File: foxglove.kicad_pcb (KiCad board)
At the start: 4 copper layers, 70.7 x 53.3 mm, 167 parts, among them IC1 LFE5U-12F-6BG256C, J1 NEIGHBOR1, J2 NEIGHBOR2, J3 Conn_02x05_Odd_Even, J4 Conn_02x10_Odd_Even, J5 Conn_01x02_Female, J6 Conn_02x03_Odd_Even, J7 BONUS_ROW, U1 LM393, U10 SHIFTER, U11 74HC4051, U12 SHIFTER, U13 74HC4051, U14 SHIFTER, U15 74HC4051, U16 SHIFTER, U17 74HC4051, U18 SHIFTER, U19 74HC4051, U2 ADP225, U20 SHIFTER, U21 74HC4051, U22 SHIFTER, U23 74HC4051, U24 SHIFTER, U25 74LVC1G53, U26 PCA6408A, U3 AP2127, U4 74LVC1G3157, U5 AP2127, U6 AP2127, U7 DAC084S085, U8 AT25xxx, U9 74HC4051

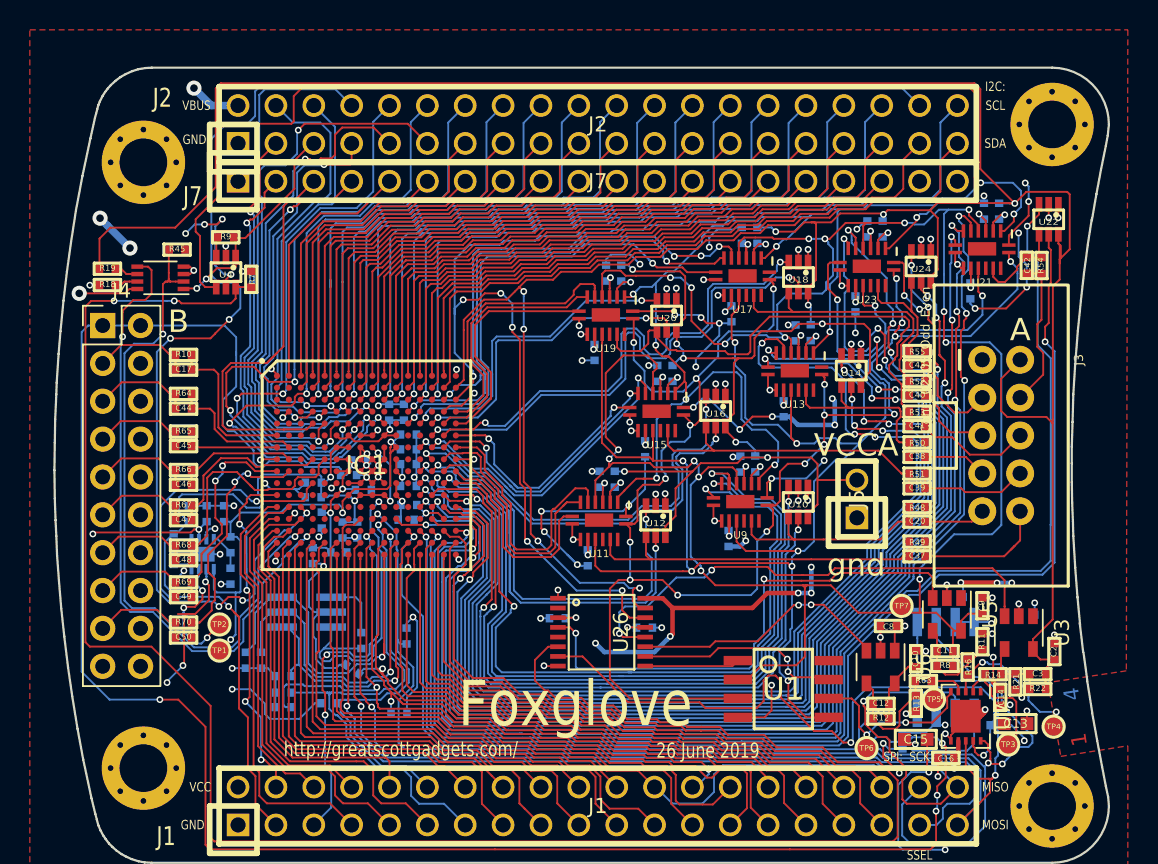
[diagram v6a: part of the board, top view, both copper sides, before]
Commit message: Matched path length of bank B differential pairs
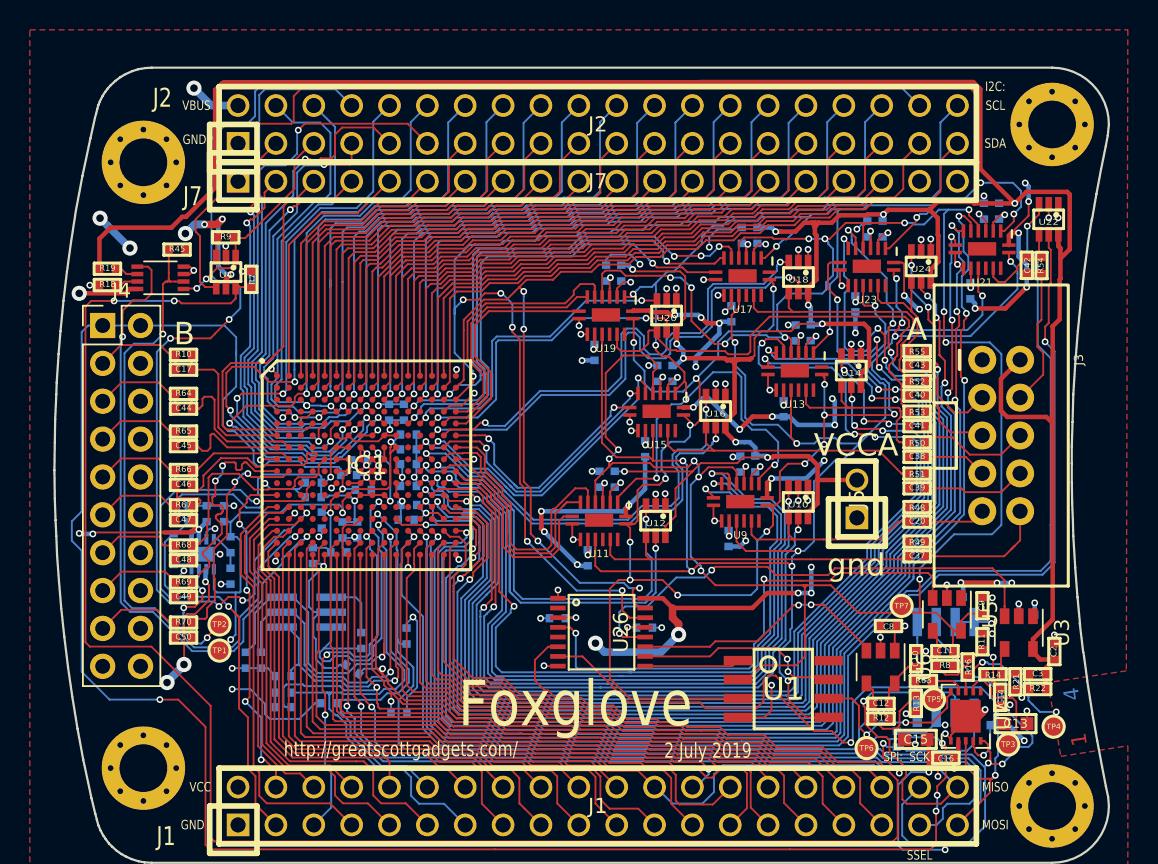
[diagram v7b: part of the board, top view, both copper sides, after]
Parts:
- moved R59 0.40 mm to (166.1, 113.6)
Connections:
- net /Sheet5D737161/target renamed /B1T_P
- net /sheet5D96E709/target renamed /B1T_N
- net /sheet5D9A1BD9/target renamed /B2T_P
- net /sheet5D9A1BDA/target renamed /B2T_N
- net /sheet5D9D50B4/target renamed /B3T_P
- net /sheet5D9D50B5/target renamed /B3T_N
- net /sheet5D9D50B6/target renamed /B4T_P
- net /sheet5D9D50B7/target renamed /B4T_N
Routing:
- net /VCCA: track 227.0 -> 263.0 mm
- net +5V: track 150.6 -> 160.2 mm, vias 52 -> 53
- net /B3_P: track 11.8 -> 15.9 mm
- net /B4_P: track 14.1 -> 16.2 mm
- net /B2_P: track 6.75 -> 8.20 mm
- net /B1_N: track 9.23 -> 10.7 mm
- net /J2.06: track 26.8 -> 26.9 mm, vias 2 -> 3
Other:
- board text added: "2 July 2019"
- board text removed: "26 June 2019"

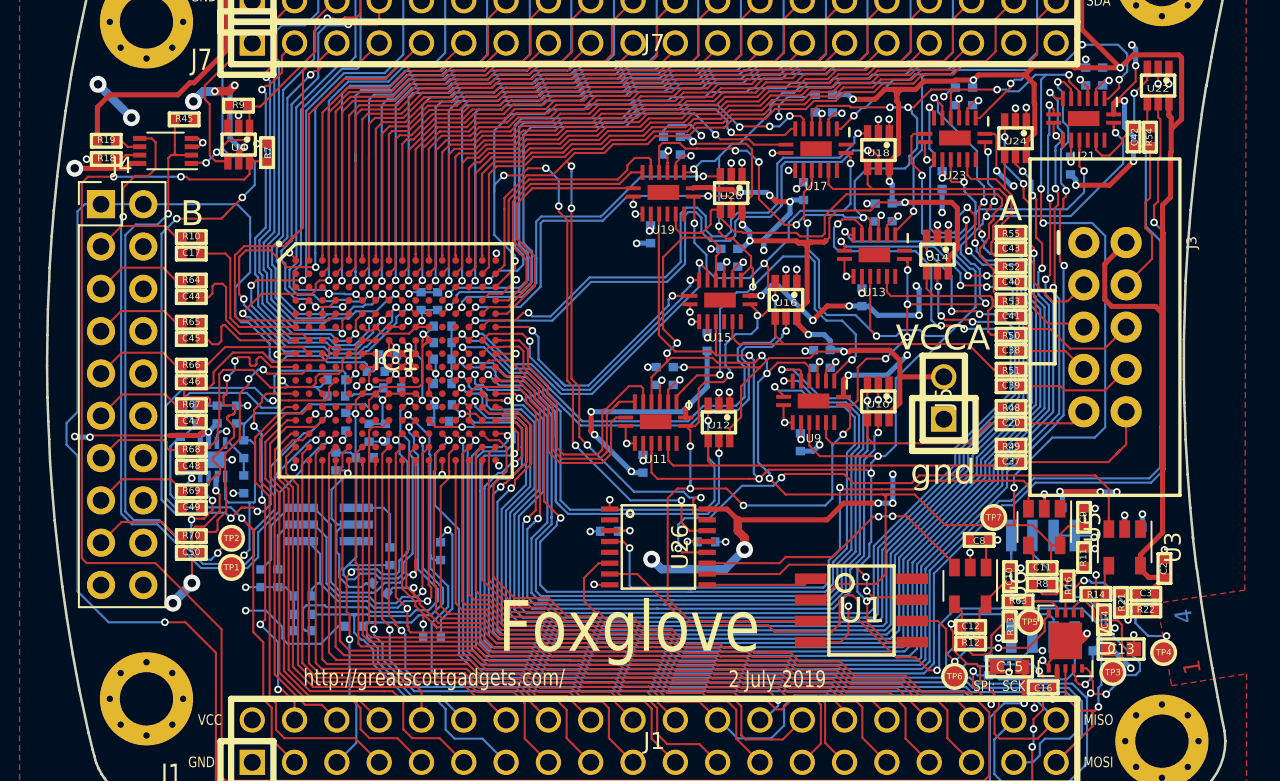
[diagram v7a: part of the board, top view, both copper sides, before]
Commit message: Changed bank A footprint and rearranged silkscreen
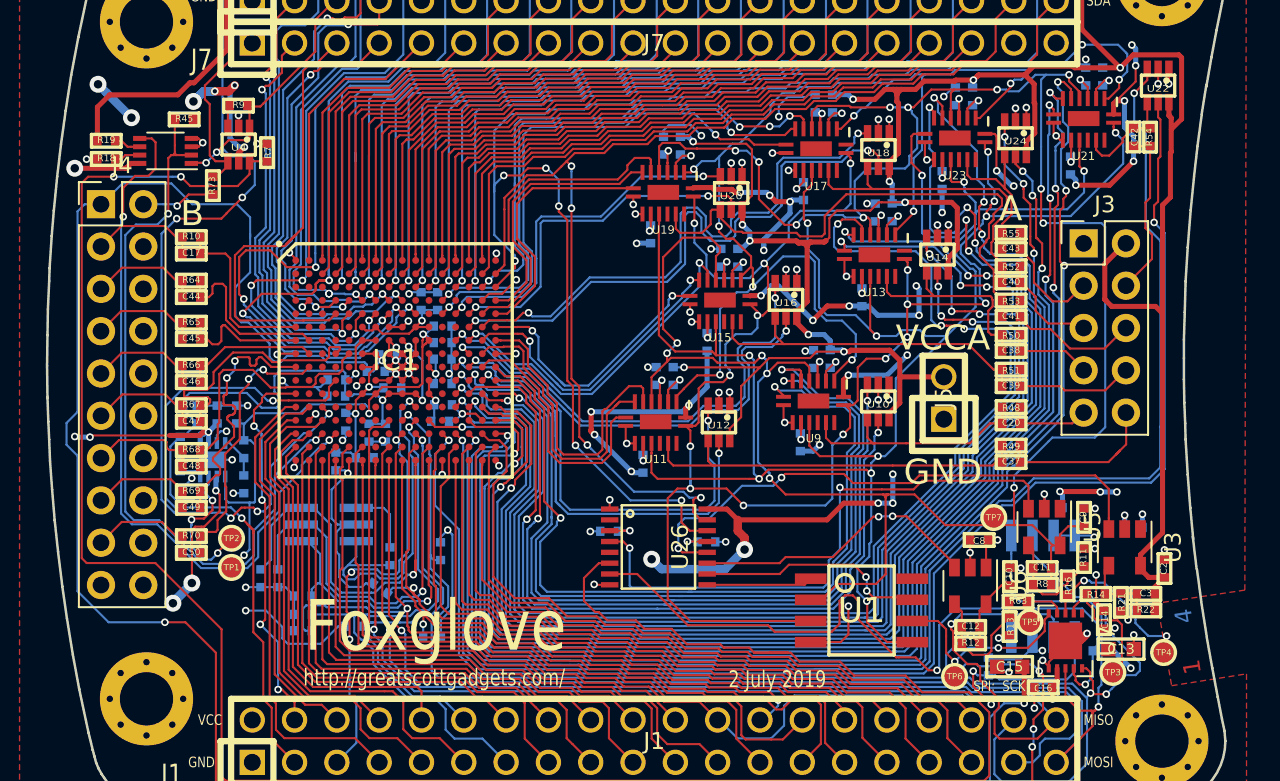
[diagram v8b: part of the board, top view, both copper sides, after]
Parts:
- added R73: 0, gsg-modules:0402, F.Cu at (119.6, 84.8)
- J3: footprint gsg-modules:2X5-SHROUDED -> Connector_PinHeader_2.54mm:PinHeader_2x05_P2.54mm_Vertical
- moved J3 5.19 mm to (171.8, 88.2)
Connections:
- J4 pad 2: /VCCB -> /Vtarget
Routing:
- net /J2.14: track 47.2 -> 60.5 mm
- net /Vtarget: track 0.00 -> 4.50 mm, vias 0 -> 1
- net /ADC_A: track 159.1 -> 160.5 mm
- net /VCCB: track 142.2 -> 143.3 mm
- net /DONE: track 24.3 -> 24.9 mm
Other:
- board text removed: "gnd"
